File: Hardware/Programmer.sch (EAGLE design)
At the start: 3 parts

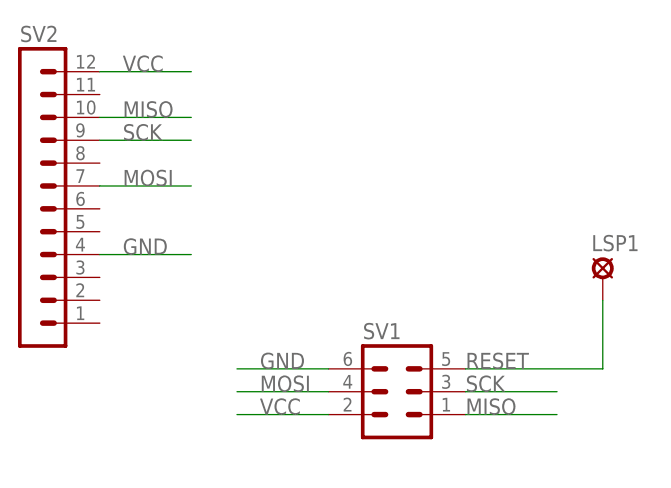
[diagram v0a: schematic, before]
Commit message: Updated missing values for connectors
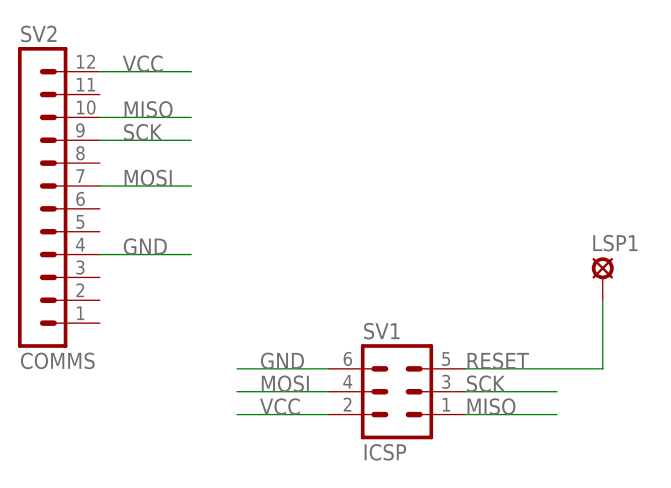
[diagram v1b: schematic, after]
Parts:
- SV1: value (none) -> ICSP
- SV2: value (none) -> COMMS
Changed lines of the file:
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@@
 <?xml version="1.0" encoding="utf-8"?>
 <!DOCTYPE eagle SYSTEM "eagle.dtd">
-<eagle version="6.5.0">
+<eagle version="6.4">
 <drawing>
 <settings>
@@
 </classes>
 <parts>
-<part name="SV1" library="con-lstb" deviceset="MA03-2" device=""/>
-<part name="SV2" library="con-lstb" deviceset="MA12-1W" device=""/>
+<part name="SV1" library="con-lstb" deviceset="MA03-2" device="" value="ICSP"/>
+<part name="SV2" library="con-lstb" deviceset="MA12-1W" device="" value="COMMS"/>
 <part name="LSP1" library="solpad" deviceset="MCS10B" device=""/>
 </parts>
